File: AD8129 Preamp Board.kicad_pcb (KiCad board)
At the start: 2 copper layers, 35 parts, among them J1 ANT, J2 TUNE, J3 TRX, T1 Transformer_1P_1S, U1 AD8129, U2 L78L06_SO8

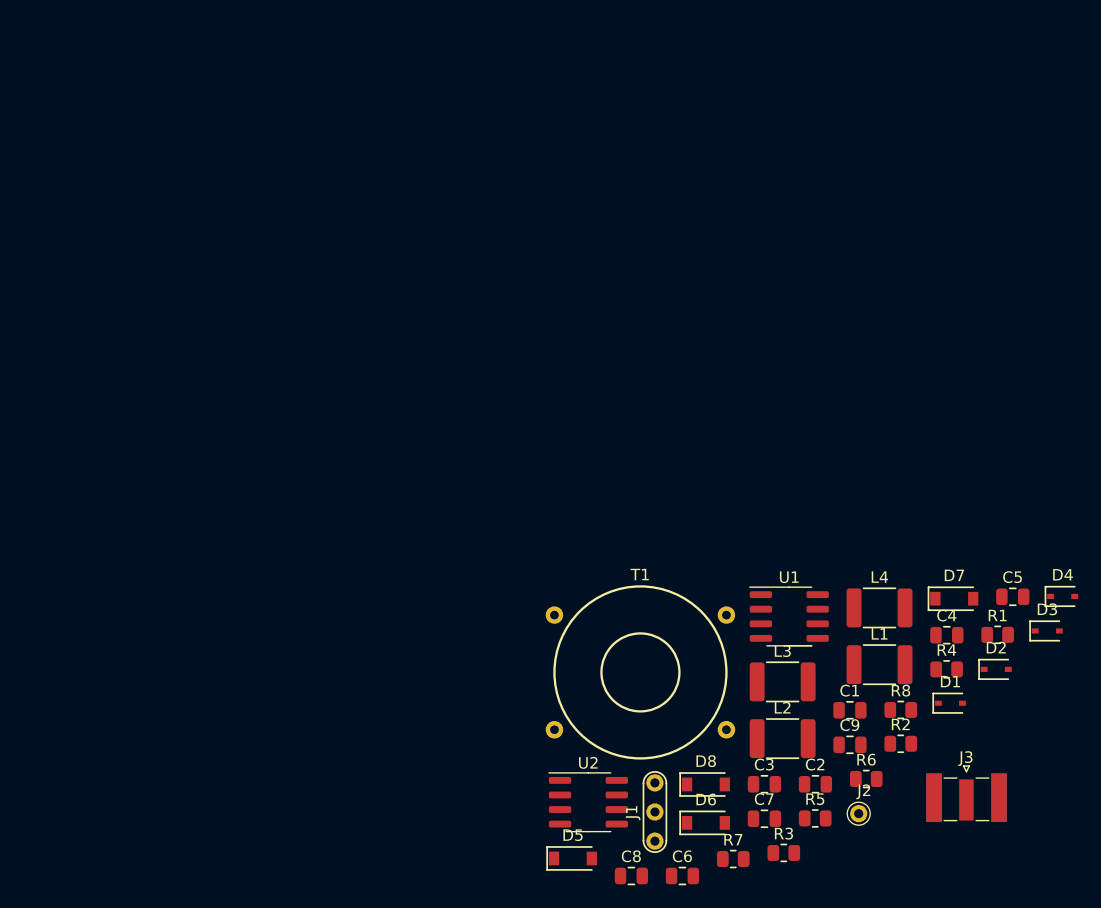
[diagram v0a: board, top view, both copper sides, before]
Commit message: ADD: pcb layout, needs via stitching
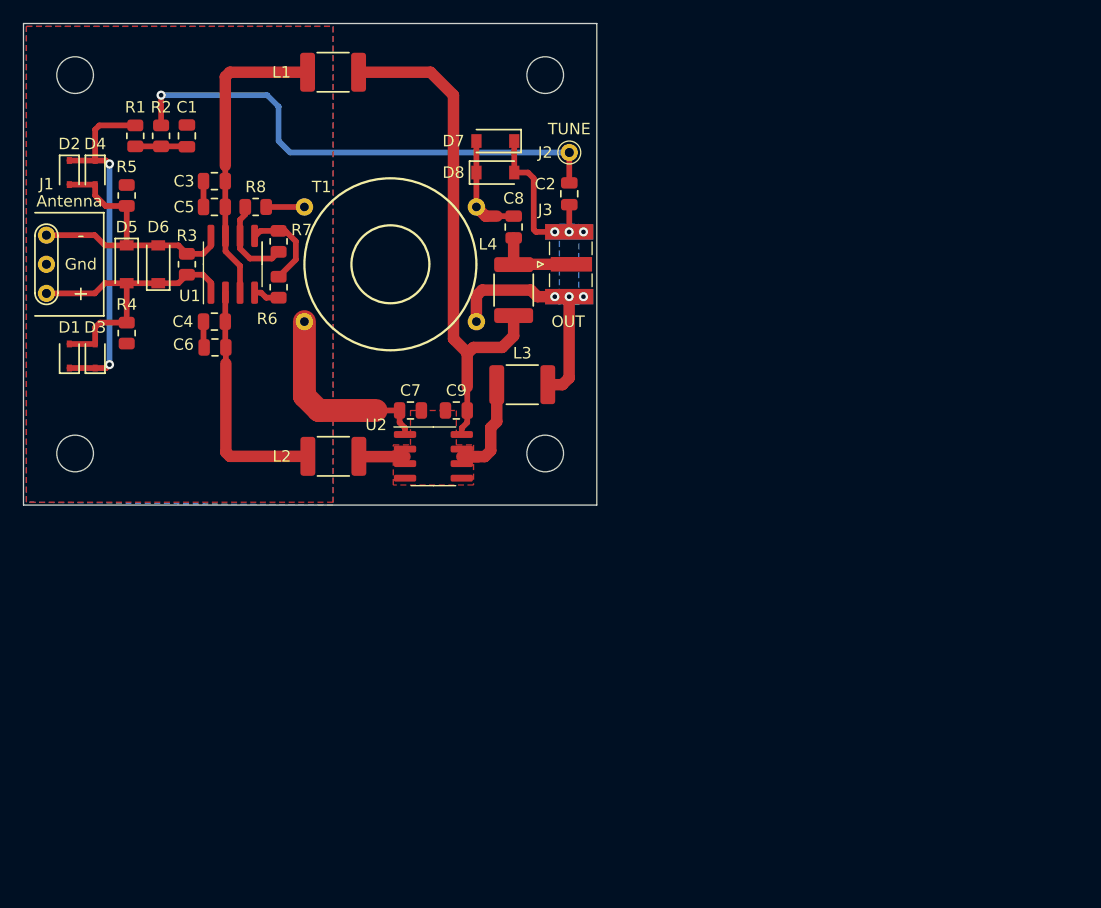
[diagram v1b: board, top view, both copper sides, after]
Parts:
- added H1: M3, AD8129 Preamp Board:MountingHole_3.2mm_M3, F.Cu at (64.5, 33.5)
- added H2: M3, AD8129 Preamp Board:MountingHole_3.2mm_M3, F.Cu at (64.5, 66.5)
- added H3: M3, AD8129 Preamp Board:MountingHole_3.2mm_M3, F.Cu at (105.5, 66.5)
- added H4: M3, AD8129 Preamp Board:MountingHole_3.2mm_M3, F.Cu at (105.5, 33.5)
- moved D4 92.1 mm to (66.2, 42.0), turned to -90 degrees
- moved D2 91.7 mm to (64.0, 42.0), turned to -90 degrees
- moved R1 86.9 mm to (69.8, 38.8), turned to -90 degrees
- moved D3 86.4 mm to (66.2, 58.0), turned to 90 degrees
- moved R2 83.5 mm to (72.0, 38.8), turned to 90 degrees
- moved D1 82.6 mm to (64.0, 58.0), turned to 90 degrees
- moved R5 81.0 mm to (69.0, 44.0), turned to 90 degrees
- moved C5 77.5 mm to (76.7, 45.0), turned to 180 degrees
- moved R4 77.3 mm to (69.0, 56.0), turned to 90 degrees
- moved C1 76.5 mm to (74.2, 38.8), turned to 90 degrees
- moved R3 73.1 mm to (74.2, 50.0), turned to 90 degrees
- moved J1 71.4 mm to (62.0, 50.0), turned to 180 degrees
- moved R8 71.3 mm to (80.2, 45.0)
- moved C3 71.2 mm to (76.7, 42.8)
- moved L1 70.3 mm to (87.0, 33.2)
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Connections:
- net Net-(C7-Pad2) renamed REGGND
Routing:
- net Net-(C9-Pad1): track 0.00 -> 45.9 mm
- net TUNE: track 0.00 -> 44.7 mm, vias 0 -> 1
- net SHLD: track 0.00 -> 34.7 mm, vias 0 -> 6
- net Net-(D1-Pad1): track 0.00 -> 31.1 mm, vias 0 -> 2
- net Net-(C3-Pad2): track 0.00 -> 26.7 mm
- net Net-(D1-Pad2): track 0.00 -> 26.2 mm
- net Net-(D2-Pad2): track 0.00 -> 25.9 mm
- net GND: track 0.00 -> 24.4 mm
- net Net-(C4-Pad1): track 0.00 -> 21.2 mm
- net REGGND: track 0.00 -> 16.0 mm
- net Net-(C8-Pad1): track 0.00 -> 9.33 mm
- net Net-(R6-Pad1): track 0.00 -> 7.86 mm
- net Net-(R7-Pad2): track 0.00 -> 7.79 mm
- net Net-(C8-Pad2): track 0.00 -> 7.37 mm
- net Net-(C1-Pad1): track 0.00 -> 4.52 mm
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- added copper zone on B.Cu, net GND
- added copper zone on F.Cu, net GND
- added copper zone on F.Cu, net REGGND
- added copper zone on B.Cu, net SHLD
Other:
- board outline added: 50 x 42 mm
- board text added: "+"
- board text added: "-"
- board text added: "Antenna"
- board text added: "Gnd"
- board text added: "OUT"
- board text added: "TUNE"
